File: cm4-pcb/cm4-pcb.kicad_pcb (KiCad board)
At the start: 2 copper layers, 140 x 70.5 mm, 41 parts, among them J1 Conn_01x02_Pin, J2 Conn_01x02_Pin, J3 USB1125-GF-B, J4 Conn_02x03_Odd_Even, J5 Conn_01x04, J6 J0011D21NL, J7 Conn_01x02, J8 Conn_01x02, J9 Conn_01x02_Pin, U1 Pfostenstecker_6_2x3, U2 Pfostenstecker_6_2x3, U5 SMD-PUSH-BTN

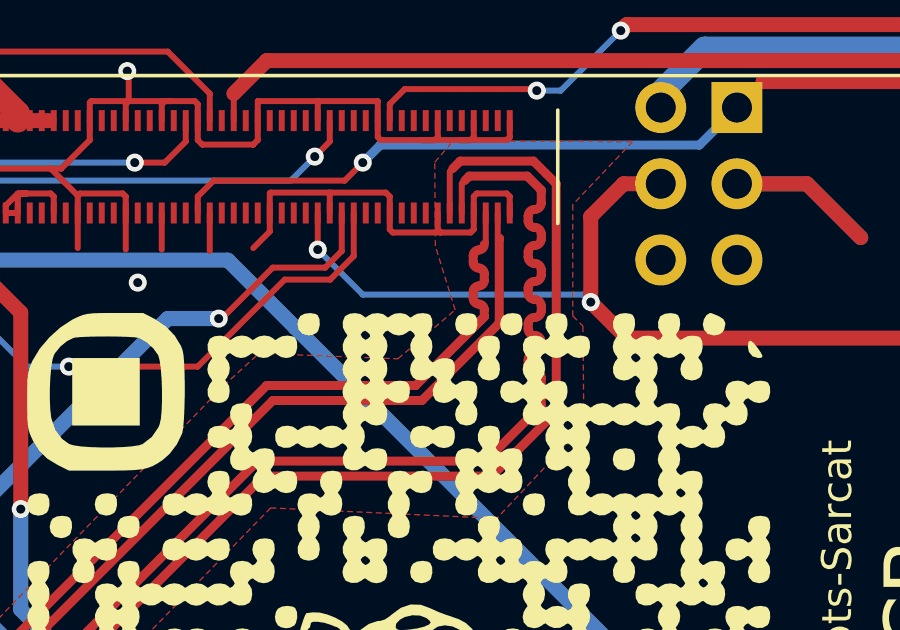
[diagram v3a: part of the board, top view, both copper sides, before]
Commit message: fixed trace length matching
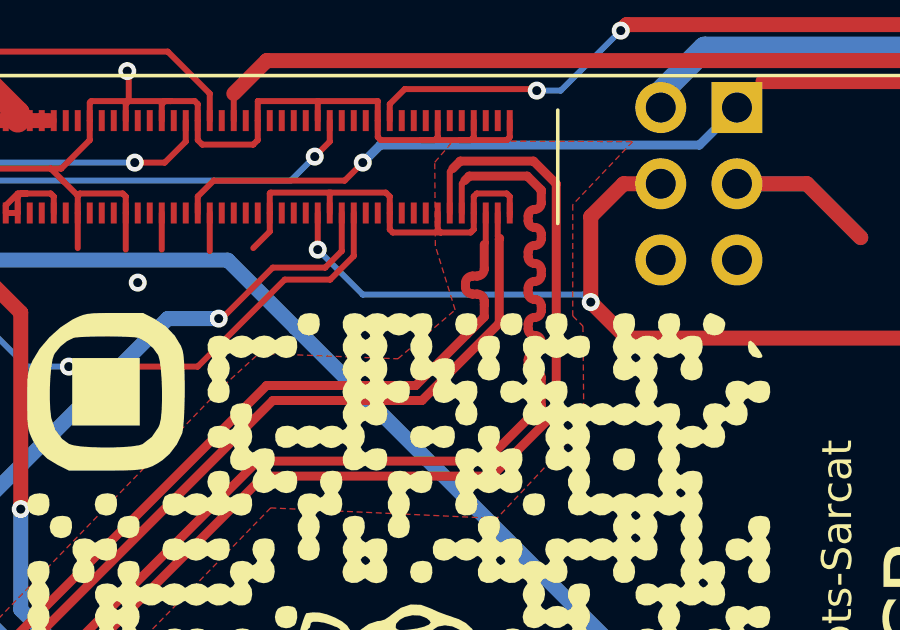
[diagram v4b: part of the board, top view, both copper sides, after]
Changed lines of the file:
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@@
 		(fp_arc
 			(start 1.390018 0.400203)
-			(mid 1.299267 0.619284)
+			(mid 1.299267 0.61928)
 			(end 1.080188 0.710033)
 			(stroke
@@
 		(fp_arc
 			(start 1.390018 0.400203)
-			(mid 1.299267 0.61928)
+			(mid 1.299267 0.619284)
 			(end 1.080188 0.710033)
 			(stroke
@@
 		(fp_arc
 			(start 1.390018 0.400203)
-			(mid 1.299267 0.619284)
+			(mid 1.299267 0.61928)
 			(end 1.080188 0.710033)
 			(stroke
@@
 	)
 	(segment
-		(start -14.403554 44.83)
-		(end -33.523554 63.95)
+		(start -7.776436 41.421686)
+		(end -7.776436 41.541686)
 		(width 0.3)
 		(layer "F.Cu")
@@
 	)
 	(segment
-		(start -33.523554 63.95)
-		(end -40.030761 63.95)
-		(width 0.3)
-		(layer "F.Cu")
-		(net 147)
-	)
-	(segment
-		(start -40.430761 63.55)
-		(end -41.999999 63.55)
+		(start -42.149999 63.7)
+		(end -42.3 63.7)
 		(width 0.3)
 		(layer "F.Cu")
@@
 	)
 	(segment
-		(start -40.030761 63.95)
-		(end -40.430761 63.55)
+		(start -7.15 42.546446)
+		(end -7.725451 43.121897)
 		(width 0.3)
 		(layer "F.Cu")
@@
 	)
 	(segment
-		(start -7.251777 42.648223)
-		(end -9.433554 44.83)
-		(width 0.3)
-		(layer "F.Cu")
-		(net 147)
-	)
-	(segment
-		(start -7.15 42.298284)
-		(end -7.15 42.53)
+		(start -7.15 42.021686)
+		(end -7.15 42.141686)
 		(width 0.3)
 		(layer "F.Cu")
@@
 	)
 	(segment
+		(start -14.403554 44.83)
+		(end -33.523554 63.95)
+		(width 0.3)
+		(layer "F.Cu")
+		(net 147)
+	)
+	(segment
 		(start -41.999999 63.55)
 		(end -42.149999 63.7)
@@
 	)
 	(segment
-		(start -9.433554 44.83)
-		(end -14.403554 44.83)
+		(start -7.15 40.13)
+		(end -7.15 40.941686)
 		(width 0.3)
 		(layer "F.Cu")
@@
 	)
 	(segment
-		(start -7.15 41.098284)
-		(end -7.15 41.33)
+		(start -40.430761 63.55)
+		(end -41.999999 63.55)
 		(width 0.3)
 		(layer "F.Cu")
@@
 	)
 	(segment
-		(start -7.15 42.546446)
-		(end -7.251777 42.648223)
-		(width 0.3)
-		(layer "F.Cu")
-		(net 147)
-	)
-	(segment
-		(start -42.149999 63.7)
-		(end -42.3 63.7)
-		(width 0.3)
-		(layer "F.Cu")
-		(net 147)
-	)
-	(segment
-		(start -7.15 42.53)
-		(end -7.15 42.546446)
+		(start -9.433554 44.83)
+		(end -14.403554 44.83)
 		(width 0.3)
 		(layer "F.Cu")
@@
 	)
 	(segment
-		(start -7.518284 41.698284)
-		(end -7.518284 41.93)
+		(start -33.523554 63.95)
+		(end -40.030761 63.95)
 		(width 0.3)
 		(layer "F.Cu")
@@
 	)
 	(segment
-		(start -7.518284 40.498284)
-		(end -7.518284 40.73)
+		(start -7.725451 43.121897)
+		(end -9.433554 44.83)
 		(width 0.3)
 		(layer "F.Cu")
 		(net 147)
 	)
-	(arc
-		(start -7.518284 41.93)
-		(mid -7.46435 42.060208)
-		(end -7.334142 42.114142)
+	(segment
+		(start -40.030761 63.95)
+		(end -40.430761 63.55)
 		(width 0.3)
 		(layer "F.Cu")
 		(net 147)
 	)
-	(arc
-		(start -7.15 41.33)
-		(mid -7.203934 41.460208)
-		(end -7.334142 41.514142)
+	(segment
+		(start -7.536436 41.781686)
+		(end -7.39 41.781686)
 		(width 0.3)
 		(layer "F.Cu")
 		(net 147)
 	)
-	(arc
-		(start -7.334142 40.314142)
-		(mid -7.46435 40.368076)
-		(end -7.518284 40.498284)
+	(segment
+		(start -7.15 42.141686)
+		(end -7.15 42.546446)
 		(width 0.3)
 		(layer "F.Cu")
 		(net 147)
 	)
-	(arc
-		(start -7.518284 40.73)
-		(mid -7.46435 40.860208)
-		(end -7.334142 40.914142)
+	(segment
+		(start -7.39 41.181686)
+		(end -7.536436 41.181686)
 		(width 0.3)
 		(layer "F.Cu")
@@
 	)
 	(arc
-		(start -7.15 40.13)
-		(mid -7.203934 40.260208)
-		(end -7.334142 40.314142)
+		(start -7.15 40.941686)
+		(mid -7.220294 41.111392)
+		(end -7.39 41.181686)
 		(width 0.3)
 		(layer "F.Cu")
@@
 	)
 	(arc
-		(start -7.334142 40.914142)
-		(mid -7.203934 40.968076)
-		(end -7.15 41.098284)
+		(start -7.39 41.781686)
+		(mid -7.220294 41.85198)
+		(end -7.15 42.021686)
 		(width 0.3)
 		(layer "F.Cu")
@@
 	)
 	(arc
-		(start -7.334142 42.114142)
-		(mid -7.203934 42.168076)
-		(end -7.15 42.298284)
+		(start -7.536436 41.181686)
+		(mid -7.706142 41.25198)
+		(end -7.776436 41.421686)
 		(width 0.3)
 		(layer "F.Cu")
@@
 	)
 	(arc
-		(start -7.334142 41.514142)
-		(mid -7.46435 41.568076)
-		(end -7.518284 41.698284)
+		(start -7.776436 41.541686)
+		(mid -7.706142 41.711392)
+		(end -7.536436 41.781686)
 		(width 0.3)
 		(layer "F.Cu")
@@
 		(base_line
 			(pts
+				(xy -7.15 40.941686) (xy -7.15 42.546446) (xy -7.725451 43.121897)
+			)
+		)
+		(base_line_coupled
+			(pts
+				(xy -6.65 40.941686) (xy -6.65 40.954013)
+			)
+		)
+		(corner_radius_percent 80)
+		(end
+			(xy -7.725451 43.121897)
+		)
+		(initial_side "right")
+		(last_diff_pair_gap 0.18)
+		(last_netname "/TRD1_N")
+		(last_status "tuned")
+		(last_track_width 0.3)
+		(last_tuning "-0.0000 mm (tuned)")
+		(max_amplitude 1)
+		(min_amplitude 0.2)
+		(min_spacing 0.6)
+		(origin
+			(xy -7.15 40.941686)
+		)
+		(override_custom_rules no)
+		(rounded yes)
+		(single_sided no)
+		(target_length 1000000)
+		(target_length_max 1000000.1)
+		(target_length_min 999999.9)
+		(target_skew 0)
+		(target_skew_max 0.1)
+		(target_skew_min -0.1)
+		(tuning_mode "diff_pair_skew")
+		(members 06596941-aa6e-43cd-945d-eaf4ca1dbae7 16ba1a1a-96d2-46c3-959c-719733521343
+			2d1d043b-84fd-4354-af2e-9a80033863c2 39123a82-e931-4df7-98c7-bf6b49d0e35b
+			3f8d265c-3dfc-4a15-8796-708362c7bbe8 71ab84fb-b5eb-414d-872b-c03f9c144012
+			76803b62-ba26-4fc8-9d56-2f1308e6da65 edbd91d4-db8d-477c-bbbc-2faceb0daa28
+			f760e518-73c4-48ed-b7d3-94fdc0f80c94 ff277515-aa9c-4bd4-b12d-b306e4563312
+		)
+	)
+	(generated
+		(type tuning_pattern)
+		(name "Tuning Pattern")
+		(layer "F.Cu")
+		(base_line
+			(pts
 				(xy -35.8 59.15) (xy -37.482213 59.15)
 			)
@@
 		)
 	)
-	(generated
-		(type tuning_pattern)
-		(name "Tuning Pattern")
-		(layer "F.Cu")
-		(base_line
-			(pts
-				(xy -7.15 40.13) (xy -7.15 42.546446) (xy -7.251777 42.648223)
-			)
-		)
-		(base_line_coupled
-			(pts
-				(xy -6.65 41.182703) (xy -6.65 41.210438)
-			)
-		)
-		(corner_radius_percent 80)
-		(end
-			(xy -7.251777 42.648223)
-		)
-		(initial_side "right")
-		(last_diff_pair_gap 0.18)
-		(last_netname "/TRD1_N")
-		(last_status "tuned")
-		(last_track_width 0.3)
-		(last_tuning "0.0000 mm (tuned)")
-		(max_amplitude 0.5)
-		(min_amplitude 0.2)
-		(min_spacing 0.6)
-		(origin
-			(xy -7.15 40.13)
-		)
-		(override_custom_rules no)
-		(rounded yes)
-		(single_sided no)
-		(target_length 1000000)
-		(target_length_max 1000000.1)
-		(target_length_min 999999.9)
-		(target_skew 0)
-		(target_skew_max 2147.483647)
-		(target_skew_min 0)
-		(tuning_mode "diff_pair_skew")
-		(members 08a0ce4c-9dbc-4067-a3a8-e87b9943b050 0fbdda6b-9871-4887-ac59-faa765e28b09
-			26891050-744d-40c2-988f-f928f1099077 2ca990a3-f7de-4ff0-bb89-897f4985fd05
-			505e0869-8fce-4688-88d1-749a16daba8f 5ef70eba-6205-4892-a705-c3ee30d58f46
-			88759b40-306f-4350-ad8d-d5de821055f3 9c8cc4d3-921c-48df-9d25-0044d1b89147
-			a4080fca-5fd8-44bc-ba4a-9e9ebedc513a b4f3dd1a-36b6-4e1e-b17b-c1e749076057
-			b711bfdf-408a-4af0-a15d-c2c2e741c3a0 c008754b-e79e-4e01-afbb-381e3f3eccd0
-			e1852efe-1e38-452c-9ea7-e0eb93a3e542 eb84f41c-5159-4833-b9ef-d69b4dc8d6f5
-		)
-	)

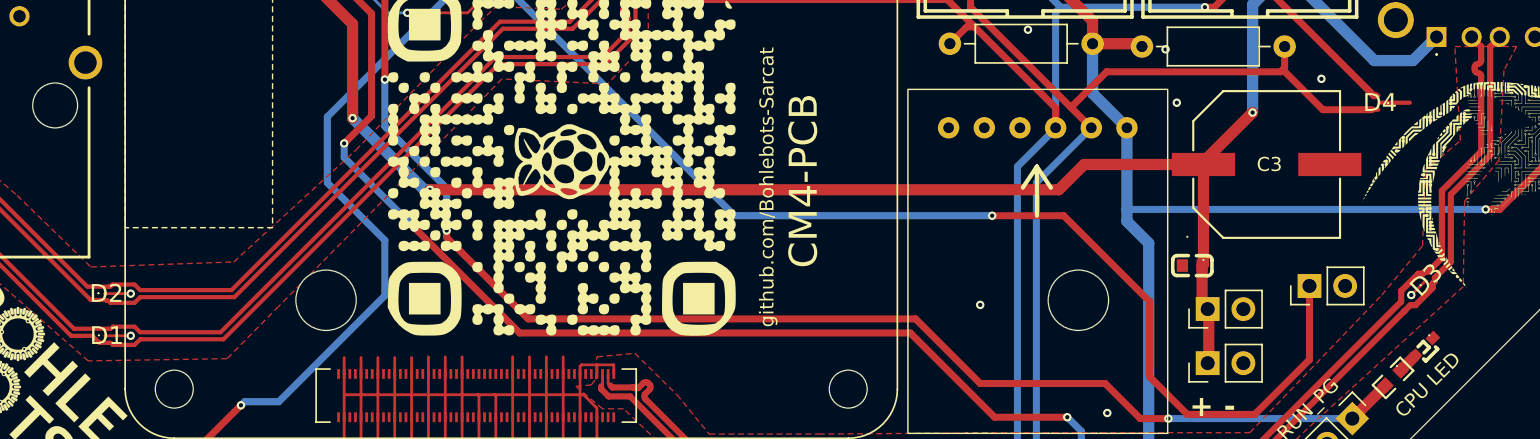
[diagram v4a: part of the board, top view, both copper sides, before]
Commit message: Added AN Pullup resistor
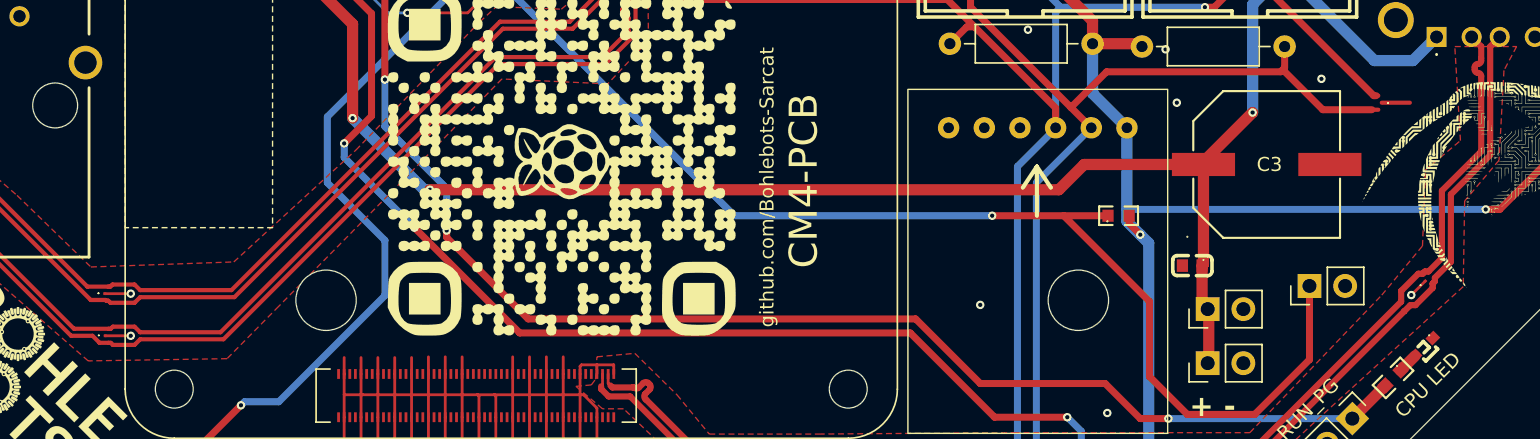
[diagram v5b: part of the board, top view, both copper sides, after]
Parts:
- added R7: SMD-10k, BohleBots:R0603, F.Cu at (29.7, 58.6)
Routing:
- net A1: track 93.2 -> 96.3 mm
- net +3.3V: track 194.5 -> 196.2 mm, vias 1 -> 2
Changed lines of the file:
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@@
 	(footprint "BohleBots:R0603"
 		(layer "F.Cu")
+		(at 29.653366 58.65)
+		(descr "R0603 footprint")
+		(tags "R0603 footprint")
+		(property "Reference" "R7"
+			(at 0 -2.660605 0)
+			(layer "F.SilkS")
+			(hide yes)
+			(effects
+				(font
+					(size 1 1)
+					(thickness 0.15)
+				)
+			)
+		)
+		(property "Value" "SMD-10k"
+			(at 0 2.660605 0)
+			(layer "F.Fab")
+			(effects
+				(font
+					(size 1 1)
+					(thickness 0.15)
+				)
+			)
+		)
+		(property "Footprint" "BohleBots:R0603"
+			(at 0 0 0)
+			(unlocked yes)
+			(layer "F.Fab")
+			(hide yes)
+			(effects
+				(font
+					(size 1.27 1.27)
+				)
+			)
+		)
+		(property "Datasheet" "https://www.mouser.in/datasheet/2/447/PYu_RT_1_to_0_01_RoHS_L_11-1669912.pdf"
+			(at 0 0 0)
+			(unlocked yes)
+			(layer "F.Fab")
+			(hide yes)
+			(effects
+				(font
+					(size 1.27 1.27)
+				)
+			)
+		)
+		(property "Description" ""
+			(at 0 0 0)
+			(unlocked yes)
+			(layer "F.Fab")
+			(hide yes)
+			(effects
+				(font
+					(size 1.27 1.27)
+				)
+			)
+		)
+		(property "LCSC" "C25804"
+			(at 0 0 0)
+			(unlocked yes)
+			(layer "F.Fab")
+			(hide yes)
+			(effects
+				(font
+					(size 1 1)
+					(thickness 0.15)
+				)
+			)
+		)
+		(sheetname "Root")
+		(sheetfile "cm4-pcb.kicad_sch")
+		(attr through_hole)
+		(fp_line
+			(start -1.38509 -0.660605)
+			(end -0.426213 -0.660605)
+			(stroke
+				(width 0.1524)
+				(type solid)
+			)
+			(layer "F.SilkS")
+		)
+		(fp_line
+			(start -1.38509 0.660605)
+			(end -1.38509 -0.660605)
+			(stroke
+				(width 0.1524)
+				(type solid)
+			)
+			(layer "F.SilkS")
+		)
+		(fp_line
+			(start -0.426213 0.660605)
+			(end -1.38509 0.660605)
+			(stroke
+				(width 0.1524)
+				(type solid)
+			)
+			(layer "F.SilkS")
+		)
+		(fp_line
+			(start 0.426213 0.660605)
+			(end 1.38509 0.660605)
+			(stroke
+				(width 0.1524)
+				(type solid)
+			)
+			(layer "F.SilkS")
+		)
+		(fp_line
+			(start 1.38509 -0.660605)
+			(end 0.426213 -0.660605)
+			(stroke
+				(width 0.1524)
+				(type solid)
+			)
+			(layer "F.SilkS")
+		)
+		(fp_line
+			(start 1.38509 0.660605)
+			(end 1.38509 -0.660605)
+			(stroke
+				(width 0.1524)
+				(type solid)
+			)
+			(layer "F.SilkS")
+		)
+		(fp_circle
+			(center -0.800102 0.400051)
+			(end -0.77013 0.400051)
+			(stroke
+				(width 0.059995)
+				(type solid)
+			)
+			(fill none)
+			(layer "F.SilkS")
+		)
+		(fp_text user "REF**"
+			(at 0 4.660605 0)
+			(layer "F.Fab")
+			(effects
+				(font
+					(size 1 1)
+					(thickness 0.15)
+				)
+			)
+		)
+		(pad "1" smd rect
+			(at -0.753366 0)
+			(size 0.806477 0.864008)
+			(layers "F.Cu" "F.Paste" "F.Mask")
+			(net 94 "A1")
+			(pinfunction "1")
+			(pintype "unspecified")
+		)
+		(pad "2" smd rect
+			(at 0.753366 0)
+			(size 0.806477 0.864008)
+			(layers "F.Cu" "F.Paste" "F.Mask")
+			(net 4 "+3.3V")
+			(pinfunction "2")
+			(pintype "unspecified")
+		)
+		(model "/home/roland/Roboter/bohlebots/Coachdaten/KiCad/scripts/JLCPCB2KiCad/bin/../../../Bohlebots_lib//footprint/packages3d/R0603.wrl"
+			(offset
+				(xyz -0.004952999926 0 0.009905999851)
+			)
+			(scale
+				(xyz 1 1 1)
+			)
+			(rotate
+				(xyz 0 0 -90)
+			)
+		)
+	)
+	(footprint "BohleBots:R0603"
+		(layer "F.Cu")
 		(at 49.2 70.2 -135)
 		(descr "R0603 footprint")
@@
 			(at 0 0 0)
 			(layer "F.SilkS")
+			(hide yes)
 			(effects
 				(font
@@
 			(at 0 0 0)
 			(layer "F.SilkS")
+			(hide yes)
 			(effects
 				(font
@@
 			(at 0 0 45)
 			(layer "F.SilkS")
+			(hide yes)
 			(effects
 				(font
@@
 			(at 0 0 180)
 			(layer "F.SilkS")
+			(hide yes)
 			(effects
 				(font
@@
 	)
 	(segment
+		(start 30.406732 58.65)
+		(end 30.406732 59.206732)
+		(width 0.5)
+		(layer "F.Cu")
+		(net 4)
+	)
+	(segment
 		(start 25.8 42.770003)
 		(end 27.8 44.770003)
@@
 	)
 	(segment
+		(start 30.406732 59.206732)
+		(end 31.2 60)
+		(width 0.5)
+		(layer "F.Cu")
+		(net 4)
+	)
+	(segment
 		(start 34.959995 42.770003)
 		(end 36.459995 41.270003)
@@
 		(net 4)
 	)
+	(via
+		(at 31.2 60)
+		(size 0.6)
+		(drill 0.3)
+		(layers "F.Cu" "B.Cu")
+		(net 4)
+	)
 	(segment
 		(start 27.8 49.938)
@@
 	)
 	(segment
+		(start 31.2 60)
+		(end 30.25 59.05)
+		(width 0.8)
+		(layer "B.Cu")
+		(net 4)
+	)
+	(segment
 		(start 12.789992 33.6)
 		(end 0.2 33.6)
@@
 	)
 	(segment
-		(start 31.8 60.6)
-		(end 30.25 59.05)
+		(start 30.25 59.05)
+		(end 30.25 58.2)
 		(width 0.8)
 		(layer "B.Cu")
@@
 	)
 	(segment
-		(start 30.25 59.05)
-		(end 30.25 58.2)
+		(start 31.8 60.6)
+		(end 31.2 60)
 		(width 0.8)
 		(layer "B.Cu")
@@
 		(width 0.5)
 		(layer "F.Cu")
+		(net 94)
+	)
+	(segment
+		(start 25.75 58.65)
+		(end 28.9 58.65)
+		(width 0.5)
+		(layer "F.Cu")

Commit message: JLCPCB Assemly
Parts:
- removed D1, D2, D3, D4: ESD122DMYR, ESD122DMYR:ESD122DMYR
- added U3: ESD122DMYR, BohleBots:X2SON-3_L1.3-W0.6-L, F.Cu at (-42.1, 67.2)
- added U4: ESD122DMYR, BohleBots:X2SON-3_L1.3-W0.6-L, F.Cu at (-42.1, 64.2)
- added U6: ESD122DMYR, BohleBots:X2SON-3_L1.3-W0.6-L, F.Cu at (50.2, 63.2)
- added U7: ESD122DMYR, BohleBots:X2SON-3_L1.3-W0.6-L, F.Cu at (48.9, 50.6)
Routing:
- net GND: track 236.7 -> 232.1 mm
- net SCL: track 182.3 -> 183.2 mm
- net SDA: track 191.4 -> 192.2 mm

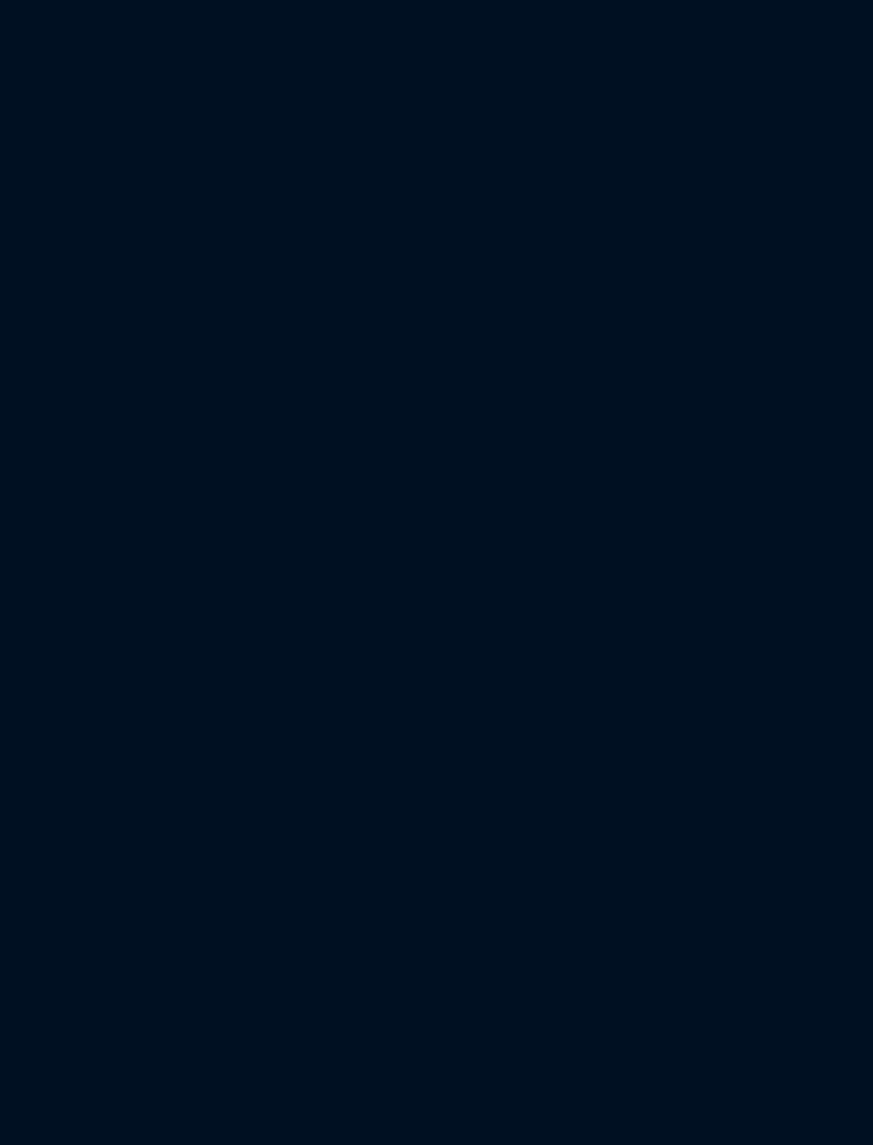
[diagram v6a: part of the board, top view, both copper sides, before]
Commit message: Added visual cm4 footprint to sarcat library
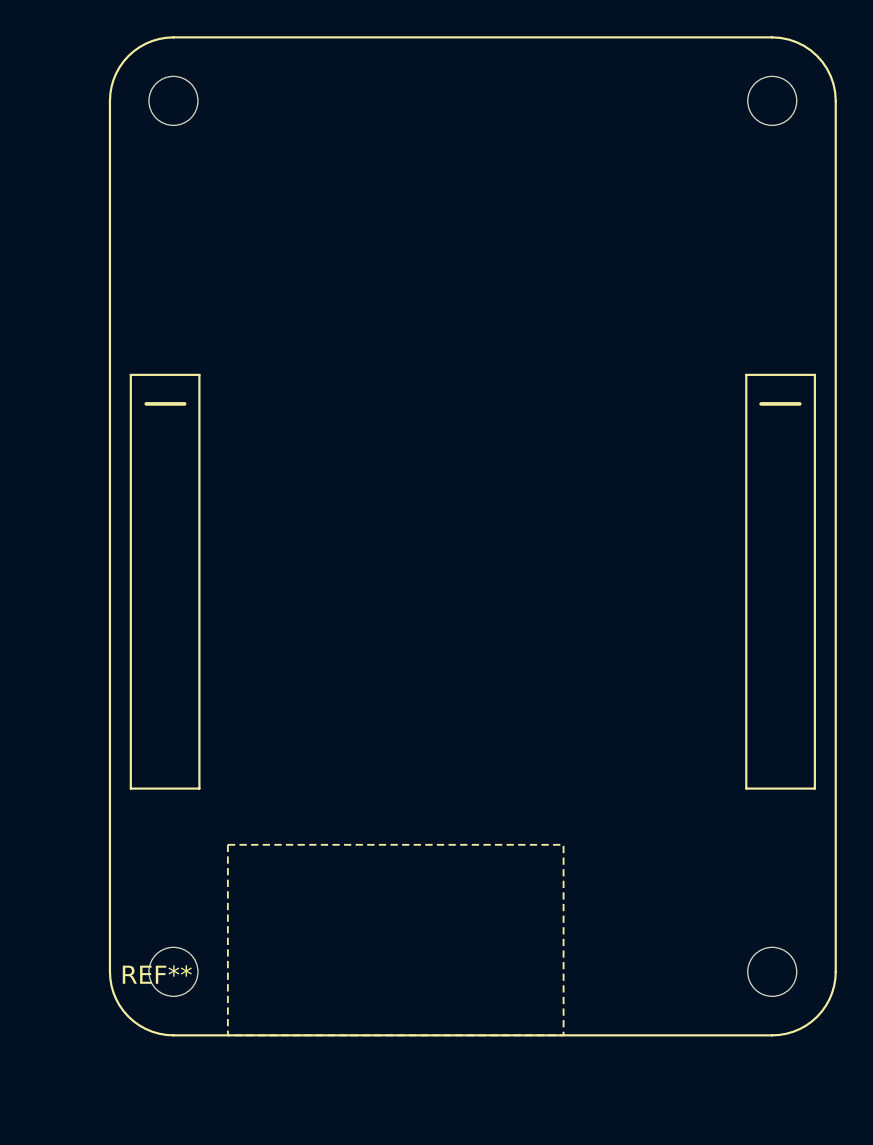
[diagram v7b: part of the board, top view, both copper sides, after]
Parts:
- added REF**: CM4-sarcat, sarcat:CM4-sarcat, F.Cu at (128.5, 64.5)
